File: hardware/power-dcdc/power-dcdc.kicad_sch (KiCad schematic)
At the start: 79 parts, among them J1 SOLAR_IN, J2 DCDC-MEASURES, J3 DCDC-PWM, J4 BATT2, J5 BATT1, Q1 SIR164ADP, Q2 SIR164ADP, Q3 SI7149ADP, Q4 SI7149ADP, Q5 SI7149ADP, Q6 SI7149ADP, Q7 BSS123, Q8 BSS123, U1 LP4951C, U2 NCP5901B, U3 PAC1953-1, U4 DGD0215, U5 DGD0215

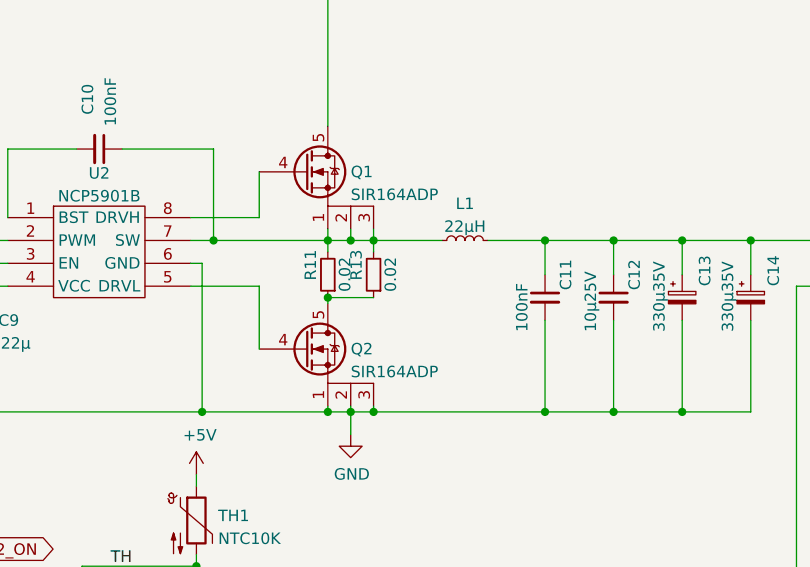
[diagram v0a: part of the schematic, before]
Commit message: Switch to a 60V N-channel mosfet on input, to have some margin.
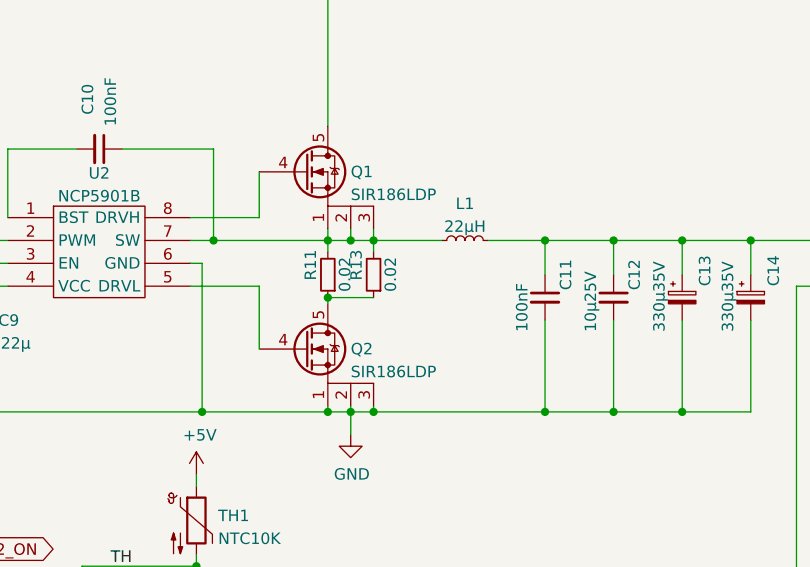
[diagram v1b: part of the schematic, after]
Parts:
- Q1, Q2: value SIR164ADP -> SIR186LDP; P/N SIR164ADP-T1-GE3 (F) -> SIR186LDP-T1-RE3
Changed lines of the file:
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@@
       (effects (font (size 1.27 1.27)) (justify left))
     )
-    (property "Value" "SIR164ADP" (id 1) (at 160.02 73.025 0)
+    (property "Value" " SIR186LDP" (id 1) (at 160.02 73.025 0)
       (effects (font (size 1.27 1.27)) (justify left))
     )
@@
       (effects (font (size 1.27 1.27)) hide)
     )
-    (property "P/N" "SIR164ADP-T1-GE3 (F)" (id 4) (at 154.94 70.485 0)
+    (property "P/N" " SIR186LDP-T1-RE3 " (id 4) (at 154.94 70.485 0)
       (effects (font (size 1.27 1.27)) hide)
     )
@@
       (effects (font (size 1.27 1.27)) (justify left))
     )
-    (property "Value" "SIR164ADP" (id 1) (at 160.02 53.34 0)
+    (property "Value" " SIR186LDP" (id 1) (at 160.02 53.34 0)
       (effects (font (size 1.27 1.27)) (justify left))
     )
@@
       (effects (font (size 1.27 1.27)) hide)
     )
-    (property "P/N" "SIR164ADP-T1-GE3 (F)" (id 4) (at 154.94 50.8 0)
+    (property "P/N" " SIR186LDP-T1-RE3" (id 4) (at 154.94 50.8 0)
       (effects (font (size 1.27 1.27)) hide)
     )
@@
     )
     (path "/32a33d85-9b2f-4588-a967-1cbb50b97c1f"
-      (reference "Q1") (unit 1) (value "SIR164ADP") (footprint "Package_SO:PowerPAK_SO-8_Single")
+      (reference "Q1") (unit 1) (value " SIR186LDP") (footprint "Package_SO:PowerPAK_SO-8_Single")
     )
     (path "/1ece4681-902d-43b4-9dc0-64cb9b75d533"
-      (reference "Q2") (unit 1) (value "SIR164ADP") (footprint "Package_SO:PowerPAK_SO-8_Single")
+      (reference "Q2") (unit 1) (value " SIR186LDP") (footprint "Package_SO:PowerPAK_SO-8_Single")
     )
     (path "/61876616-a212-4edc-ba55-98c0b1bf2dee"

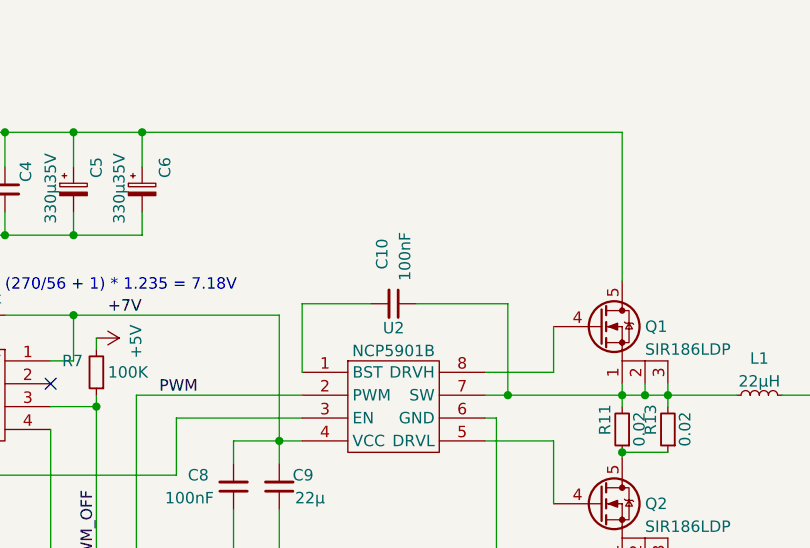
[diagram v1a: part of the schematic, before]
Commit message: Provision for a second bootstrap capacitor
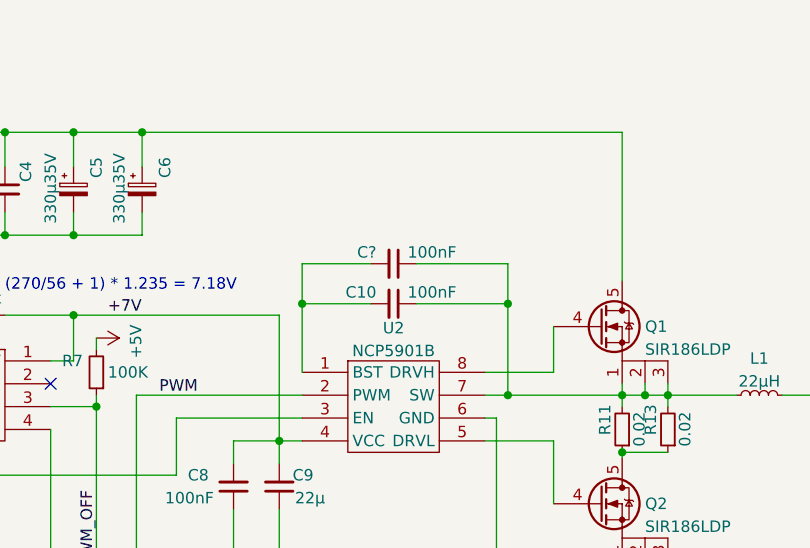
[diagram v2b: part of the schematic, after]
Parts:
- added C?: 100nF, Capacitor_SMD:C_0603_1608Metric_Pad1.08x0.95mm_HandSolder, symbol Device:C_Small
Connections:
- net at C10.1, L1.1, Q1.1 (S)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: now also C?.1
- net at C10.2, U2.1 (BST): now also C?.2
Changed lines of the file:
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@@
   (junction (at 271.78 87.63) (diameter 0) (color 0 0 0 0)
   )
+  (junction (at 144.78 48.26) (diameter 0) (color 0 0 0 0)
+  )
   (junction (at 238.125 106.68) (diameter 0) (color 0 0 0 0)
   )
@@
   (junction (at 157.48 58.42) (diameter 0) (color 0 0 0 0)
   )
+  (junction (at 121.92 48.26) (diameter 0) (color 0 0 0 0)
+  )
   (junction (at 269.24 76.2) (diameter 0) (color 0 0 0 0)
   )
@@
     (stroke (width 0) (type default) (color 0 0 0 0))
   )
+  (wire (pts (xy 121.92 43.815) (xy 121.92 48.26))
+    (stroke (width 0) (type default) (color 0 0 0 0))
+  )
   (wire (pts (xy 62.23 29.21) (xy 62.23 54.61))
     (stroke (width 0) (type default) (color 0 0 0 0))
@@
     (stroke (width 0) (type default) (color 0 0 0 0))
   )
+  (wire (pts (xy 144.78 43.815) (xy 144.78 48.26))
+    (stroke (width 0) (type default) (color 0 0 0 0))
+  )
   (wire (pts (xy 227.33 83.82) (xy 227.33 87.63))
     (stroke (width 0) (type default) (color 0 0 0 0))
@@
     (stroke (width 0) (type default) (color 0 0 0 0))
   )
+  (wire (pts (xy 129.54 43.815) (xy 121.92 43.815))
+    (stroke (width 0) (type default) (color 0 0 0 0))
+  )
   (wire (pts (xy 196.85 139.7) (xy 205.74 139.7))
     (stroke (width 0) (type default) (color 0 0 0 0))
@@
     (stroke (width 0) (type default) (color 0 0 0 0))
   )
+  (wire (pts (xy 134.62 43.815) (xy 144.78 43.815))
+    (stroke (width 0) (type default) (color 0 0 0 0))
+  )
   (wire (pts (xy 99.06 59.69) (xy 99.06 79.375))
     (stroke (width 0) (type default) (color 0 0 0 0))
@@
   (symbol (lib_id "Device:C_Small") (at 132.08 48.26 270) (unit 1)
     (in_bom yes) (on_board yes)
-    (property "Reference" "C10" (id 0) (at 130.81 44.45 0)
+    (property "Reference" "C10" (id 0) (at 130.175 46.99 90)
       (effects (font (size 1.27 1.27)) (justify right))
     )
-    (property "Value" "100nF" (id 1) (at 133.35 45.72 0)
+    (property "Value" "100nF" (id 1) (at 139.065 46.99 90)
       (effects (font (size 1.27 1.27)) (justify right))
     )
@@
     (pin "5")
   )
+  (symbol (lib_id "Device:C_Small") (at 132.08 43.815 270) (unit 1)
+    (in_bom yes) (on_board yes)
+    (property "Reference" "C?" (id 0) (at 130.175 42.545 90)
+      (effects (font (size 1.27 1.27)) (justify right))
+    )
+    (property "Value" "100nF" (id 1) (at 139.065 42.545 90)
+      (effects (font (size 1.27 1.27)) (justify right))
+    )
+    (property "Footprint" "Capacitor_SMD:C_0603_1608Metric_Pad1.08x0.95mm_HandSolder" (id 2) (at 132.08 43.815 0)
+      (effects (font (size 1.27 1.27)) hide)
+    )
+    (property "Datasheet" "~" (id 3) (at 132.08 43.815 0)
+      (effects (font (size 1.27 1.27)) hide)
+    )
+    (property "P/N" "MC0603B104K250CT (stock)" (id 4) (at 132.08 43.815 0)
+      (effects (font (size 1.27 1.27)) hide)
+    )
+    (pin "1")
+    (pin "2")
+  )
   (symbol (lib_id "Device:R_Small") (at 271.78 125.095 0) (unit 1)
     (in_bom yes) (on_board yes) (fields_autoplaced)
@@
       (reference "C19") (unit 1) (value "100nF") (footprint "Capacitor_SMD:C_0603_1608Metric_Pad1.08x0.95mm_HandSolder")
     )
+    (path "/6399bf34-9cd9-4724-9127-2e3430db67f3"
+      (reference "C?") (unit 1) (value "100nF") (footprint "Capacitor_SMD:C_0603_1608Metric_Pad1.08x0.95mm_HandSolder")
+    )
     (path "/b97d5a53-2424-4463-9f29-8a4d0e12cc96"

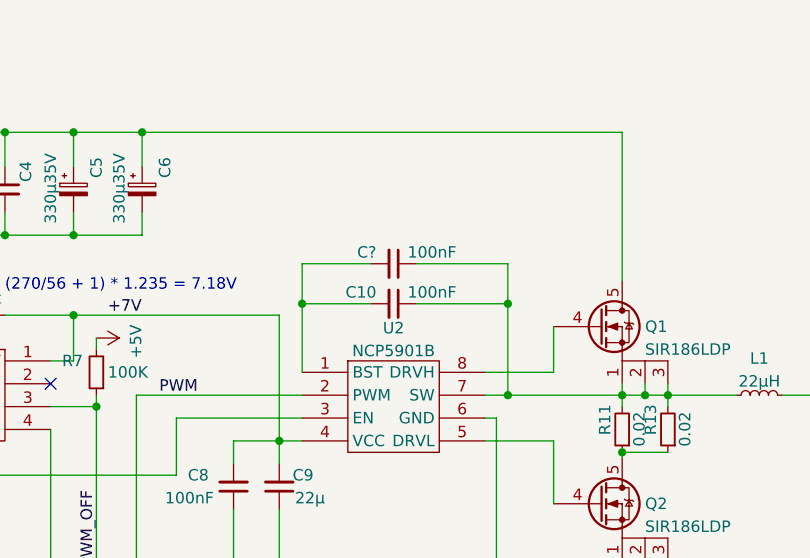
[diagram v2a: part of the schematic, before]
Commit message: On second through use a 1µF capacitor for bootstrap
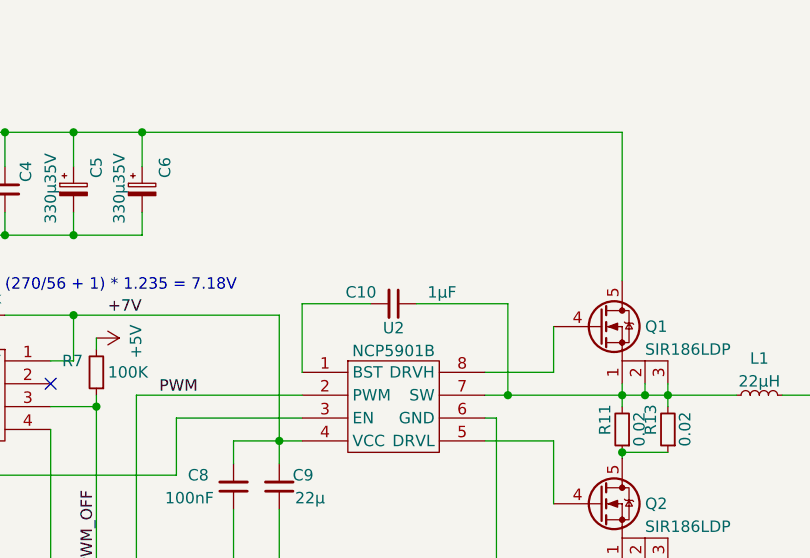
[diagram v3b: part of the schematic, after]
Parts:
- removed C?: 100nF, Capacitor_SMD:C_0603_1608Metric_Pad1.08x0.95mm_HandSolder, symbol Device:C_Small
- C10: value 100nF -> 1µF; footprint Capacitor_SMD:C_0603_1608Metric_Pad1.08x0.95mm_HandSolder -> Capacitor_SMD:C_0805_2012Metric_Pad1.18x1.45mm_HandSolder; P/N MC0603B104K250CT (stock) -> 08053C105KAT2A
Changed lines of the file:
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@@
   (junction (at 271.78 87.63) (diameter 0) (color 0 0 0 0)
   )
-  (junction (at 144.78 48.26) (diameter 0) (color 0 0 0 0)
-  )
   (junction (at 238.125 106.68) (diameter 0) (color 0 0 0 0)
   )
@@
   (junction (at 157.48 58.42) (diameter 0) (color 0 0 0 0)
   )
-  (junction (at 121.92 48.26) (diameter 0) (color 0 0 0 0)
-  )
   (junction (at 269.24 76.2) (diameter 0) (color 0 0 0 0)
   )
@@
     (stroke (width 0) (type default) (color 0 0 0 0))
   )
-  (wire (pts (xy 121.92 43.815) (xy 121.92 48.26))
-    (stroke (width 0) (type default) (color 0 0 0 0))
-  )
   (wire (pts (xy 62.23 29.21) (xy 62.23 54.61))
     (stroke (width 0) (type default) (color 0 0 0 0))
@@
     (stroke (width 0) (type default) (color 0 0 0 0))
   )
-  (wire (pts (xy 144.78 43.815) (xy 144.78 48.26))
-    (stroke (width 0) (type default) (color 0 0 0 0))
-  )
   (wire (pts (xy 227.33 83.82) (xy 227.33 87.63))
     (stroke (width 0) (type default) (color 0 0 0 0))
@@
     (stroke (width 0) (type default) (color 0 0 0 0))
   )
-  (wire (pts (xy 129.54 43.815) (xy 121.92 43.815))
-    (stroke (width 0) (type default) (color 0 0 0 0))
-  )
   (wire (pts (xy 196.85 139.7) (xy 205.74 139.7))
     (stroke (width 0) (type default) (color 0 0 0 0))
@@
     (stroke (width 0) (type default) (color 0 0 0 0))
   )
-  (wire (pts (xy 134.62 43.815) (xy 144.78 43.815))
-    (stroke (width 0) (type default) (color 0 0 0 0))
-  )
   (wire (pts (xy 99.06 59.69) (xy 99.06 79.375))
     (stroke (width 0) (type default) (color 0 0 0 0))
@@
       (effects (font (size 1.27 1.27)) (justify right))
     )
-    (property "Value" "100nF" (id 1) (at 139.065 46.99 90)
+    (property "Value" "1µF" (id 1) (at 139.065 46.99 90)
       (effects (font (size 1.27 1.27)) (justify right))
     )
-    (property "Footprint" "Capacitor_SMD:C_0603_1608Metric_Pad1.08x0.95mm_HandSolder" (id 2) (at 132.08 48.26 0)
+    (property "Footprint" "Capacitor_SMD:C_0805_2012Metric_Pad1.18x1.45mm_HandSolder" (id 2) (at 132.08 48.26 0)
       (effects (font (size 1.27 1.27)) hide)
     )
@@
       (effects (font (size 1.27 1.27)) hide)
     )
-    (property "P/N" "MC0603B104K250CT (stock)" (id 4) (at 132.08 48.26 0)
+    (property "P/N" "08053C105KAT2A" (id 4) (at 132.08 48.26 0)
       (effects (font (size 1.27 1.27)) hide)
     )
@@
     (pin "5")
   )
-  (symbol (lib_id "Device:C_Small") (at 132.08 43.815 270) (unit 1)
-    (in_bom yes) (on_board yes)
-    (property "Reference" "C?" (id 0) (at 130.175 42.545 90)
-      (effects (font (size 1.27 1.27)) (justify right))
-    )
-    (property "Value" "100nF" (id 1) (at 139.065 42.545 90)
-      (effects (font (size 1.27 1.27)) (justify right))
-    )
-    (property "Footprint" "Capacitor_SMD:C_0603_1608Metric_Pad1.08x0.95mm_HandSolder" (id 2) (at 132.08 43.815 0)
-      (effects (font (size 1.27 1.27)) hide)
-    )
-    (property "Datasheet" "~" (id 3) (at 132.08 43.815 0)
-      (effects (font (size 1.27 1.27)) hide)
-    )
-    (property "P/N" "MC0603B104K250CT (stock)" (id 4) (at 132.08 43.815 0)
-      (effects (font (size 1.27 1.27)) hide)
-    )
-    (pin "1")
-    (pin "2")
-  )
   (symbol (lib_id "Device:R_Small") (at 271.78 125.095 0) (unit 1)
     (in_bom yes) (on_board yes) (fields_autoplaced)
@@
     )
     (path "/1eca936c-8f9d-4638-b3d6-118b66dd861c"
-      (reference "C10") (unit 1) (value "100nF") (footprint "Capacitor_SMD:C_0603_1608Metric_Pad1.08x0.95mm_HandSolder")
+      (reference "C10") (unit 1) (value "1µF") (footprint "Capacitor_SMD:C_0805_2012Metric_Pad1.18x1.45mm_HandSolder")
     )
     (path "/cb60d6ca-022c-481c-8b13-485b0488b2af"
@@
       (reference "C19") (unit 1) (value "100nF") (footprint "Capacitor_SMD:C_0603_1608Metric_Pad1.08x0.95mm_HandSolder")
     )
-    (path "/6399bf34-9cd9-4724-9127-2e3430db67f3"
-      (reference "C?") (unit 1) (value "100nF") (footprint "Capacitor_SMD:C_0603_1608Metric_Pad1.08x0.95mm_HandSolder")
-    )
     (path "/b97d5a53-2424-4463-9f29-8a4d0e12cc96"

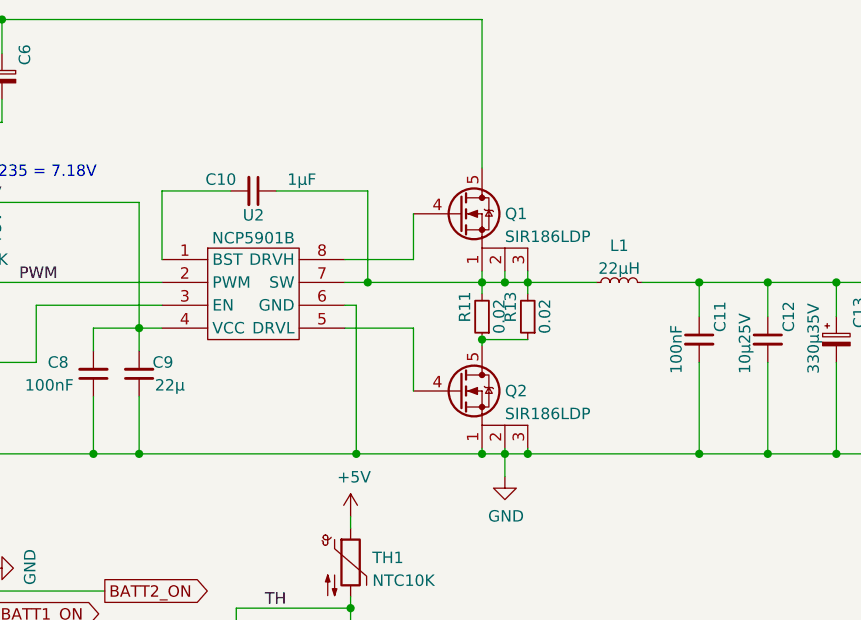
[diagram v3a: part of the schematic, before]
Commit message: Provision components to limit ringing on the sw node: A Rboot resistor and a R/C filter on the sw node.
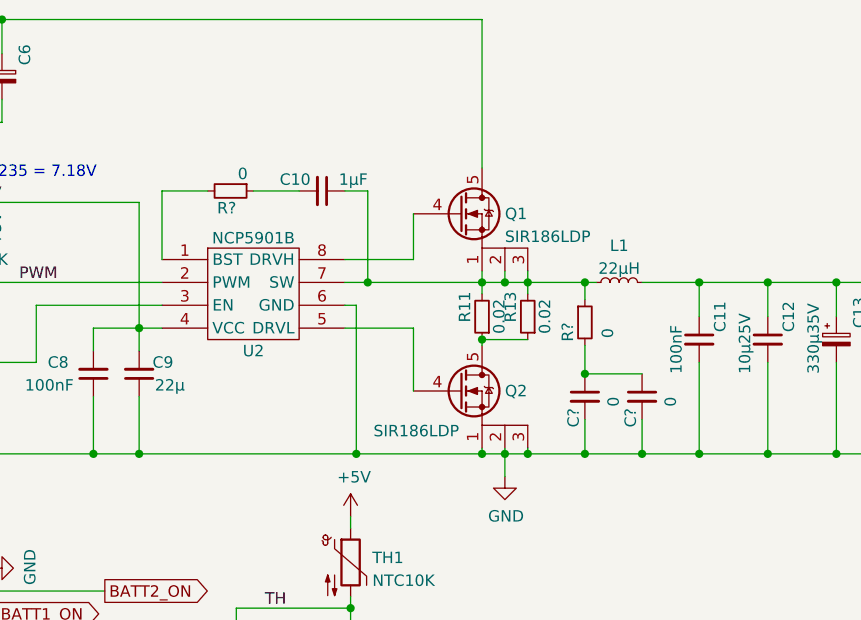
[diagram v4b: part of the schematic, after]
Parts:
- added C? (x2): 0, Capacitor_SMD:C_0805_2012Metric_Pad1.18x1.45mm_HandSolder, symbol Device:C_Small
- added R? (x2): 0, Resistor_SMD:R_1210_3225Metric_Pad1.30x2.65mm_HandSolder, symbol Device:R_Small
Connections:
- net GND: now also C?.2, C?.2
- net at C10.1, L1.1, Q1.1 (S)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: now also R?.1
- net at U2.1 (BST): now also R?.2; no longer C10.2
- new net: C10.2, R?.1
- new net: C?.1, C?.1, R?.2
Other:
- moved on the sheet: C10
